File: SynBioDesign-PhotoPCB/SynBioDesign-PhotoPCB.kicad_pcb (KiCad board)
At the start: 2 copper layers, 45 x 45 mm, 26 parts, among them IC1 OPA322SAIDBVT, J1 Conn_01x03_Male

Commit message: Adding silk
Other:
- board text added: "SynBioDesign Photodiode PCB"
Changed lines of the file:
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@@
   (gr_line (start 142.5 67.5) (end 177.5 67.5) (layer "Edge.Cuts") (width 0.1))
   (gr_arc (start 137.5 72.5) (mid 138.964466 68.964466) (end 142.5 67.5) (layer "Edge.Cuts") (width 0.1))
+  (gr_text "SynBioDesign Photodiode PCB" (at 160 107) (layer "B.SilkS")
+    (effects (font (size 1.1 1.1) (thickness 0.2)) (justify mirror))
+  )
   (segment (start 151.69 90) (end 148.69 93) (width 0.5) (layer "F.Cu") (net 1))
   (segment (start 149 104) (end 149 100) (width 1) (layer "F.Cu") (net 1))

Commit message: Bug fixes
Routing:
- net +5V: track 48.7 -> 46.4 mm
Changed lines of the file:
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@@
     (property "Sheetname" "")
     (attr through_hole)
-    (fp_text reference "D1" (at -1.776 -2.2048) (layer "F.SilkS")
+    (fp_text reference "D1" (at -4 -1) (layer "F.SilkS")
       (effects (font (size 0.48 0.48) (thickness 0.15)))
     )
@@
     (property "Sheetname" "")
     (attr smd)
-    (fp_text reference "IC1" (at 0 -2.9 90) (layer "F.SilkS")
+    (fp_text reference "IC1" (at 0 2.5 90) (layer "F.SilkS")
       (effects (font (size 1 1) (thickness 0.15)))
     )
@@
   (segment (start 158.5 86.85) (end 159.45 86.85) (width 0.5) (layer "F.Cu") (net 7))
   (segment (start 147.92 80) (end 147.92 77) (width 1) (layer "F.Cu") (net 7))
-  (segment (start 161.5 83) (end 162.5 83) (width 1) (layer "B.Cu") (net 7))
-  (segment (start 161 82.5) (end 161.5 83) (width 1) (layer "B.Cu") (net 7))
-  (segment (start 162 86.5) (end 162 83.5) (width 1) (layer "B.Cu") (net 7))
-  (segment (start 164 81.5) (end 162.5 83) (width 1) (layer "B.Cu") (net 7))
-  (segment (start 162 83.5) (end 161 82.5) (width 1) (layer "B.Cu") (net 7))
-  (segment (start 149.92 82) (end 147.92 80) (width 1) (layer "B.Cu") (net 7))
-  (segment (start 180 81.5) (end 164 81.5) (width 1) (layer "B.Cu") (net 7))
-  (segment (start 160.5 82) (end 149.92 82) (width 1) (layer "B.Cu") (net 7))
-  (segment (start 161 82.5) (end 160.5 82) (width 1) (layer "B.Cu") (net 7))
-  (segment (start 162.5 83) (end 162 83.5) (width 1) (layer "B.Cu") (net 7))
+  (segment (start 154.42 86.5) (end 147.92 80) (width 1) (layer "B.Cu") (net 7))
+  (segment (start 167 81.5) (end 162 86.5) (width 1) (layer "B.Cu") (net 7))
+  (segment (start 180 81.5) (end 167 81.5) (width 1) (layer "B.Cu") (net 7))
+  (segment (start 161.9 86.5) (end 154.42 86.5) (width 1) (layer "B.Cu") (net 7))
   (segment (start 153.77 96) (end 153.77 93) (width 1) (layer "F.Cu") (net 8))
   (segment (start 156.96 93) (end 156.96 96) (width 1) (layer "F.Cu") (net 8))

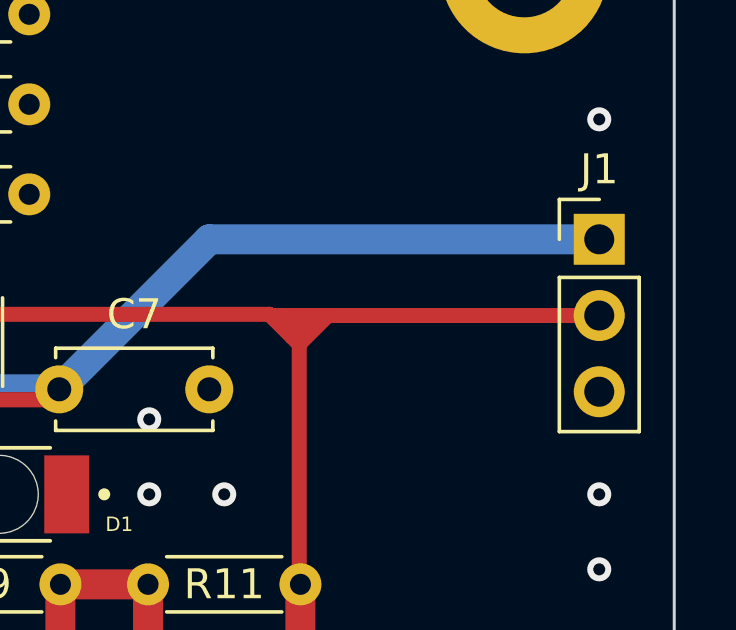
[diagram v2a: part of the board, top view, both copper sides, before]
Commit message: Added pin label silk
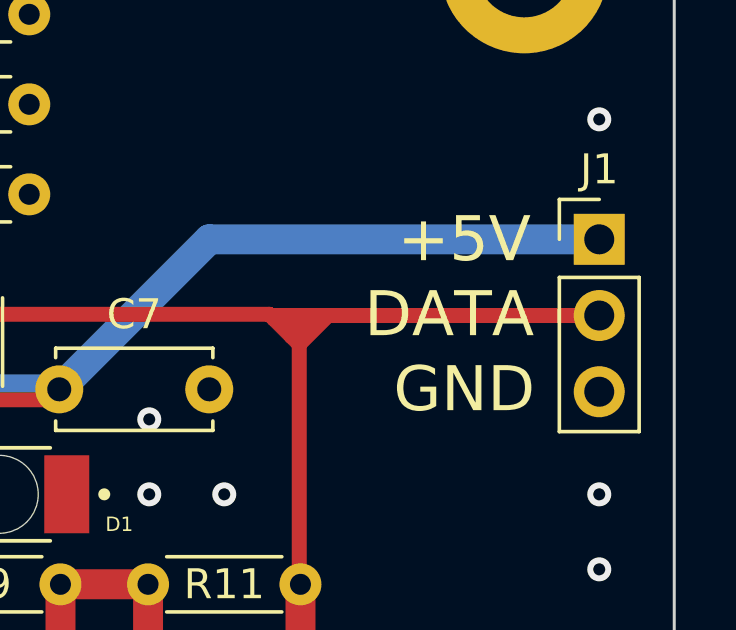
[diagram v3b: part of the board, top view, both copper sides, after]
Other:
- board text added: "+5V"
- board text added: "DATA"
- board text added: "GND"
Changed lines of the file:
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@@
   (gr_line (start 142.5 67.5) (end 177.5 67.5) (layer "Edge.Cuts") (width 0.1))
   (gr_arc (start 137.5 72.5) (mid 138.964466 68.964466) (end 142.5 67.5) (layer "Edge.Cuts") (width 0.1))
+  (gr_text "+5V" (at 174.678572 81.5) (layer "B.SilkS")
+    (effects (font (size 1.5 1.5) (thickness 0.3)) (justify mirror))
+  )
+  (gr_text "DATA" (at 175.178572 84) (layer "B.SilkS")
+    (effects (font (size 1.5 1.5) (thickness 0.3)) (justify mirror))
+  )
+  (gr_text "GND" (at 174.678572 86.5) (layer "B.SilkS")
+    (effects (font (size 1.5 1.5) (thickness 0.3)) (justify mirror))
+  )
   (gr_text "SynBioDesign Photodiode PCB" (at 160 107) (layer "B.SilkS")
     (effects (font (size 1.1 1.1) (thickness 0.2)) (justify mirror))
   )
+  (gr_text "GND" (at 175.5 86.5) (layer "F.SilkS")
+    (effects (font (size 1.5 1.5) (thickness 0.3)))
+  )
+  (gr_text "+5V" (at 175.5 81.5) (layer "F.SilkS")
+    (effects (font (size 1.5 1.5) (thickness 0.3)))
+  )
+  (gr_text "DATA" (at 175 84) (layer "F.SilkS")
+    (effects (font (size 1.5 1.5) (thickness 0.3)))
+  )
   (segment (start 151.69 90) (end 148.69 93) (width 0.5) (layer "F.Cu") (net 1))
